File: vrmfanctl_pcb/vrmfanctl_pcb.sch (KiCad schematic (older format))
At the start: 6 parts, among them J1 SATA Power Male, J2 Conn_02x03_Odd_Even, J3 Pin socket L-shape, J4 Pin socket L-shape, U1 ATtiny85-20PU

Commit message: change temperature measurement method. remove configuration interface. use printf instead of put*.
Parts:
- removed J2: Conn_02x03_Odd_Even, symbol Connector_Generic:Conn_02x03_Odd_Even
- added C2: 470p, Capacitor_THT:C_Disc_D3.0mm_W1.6mm_P2.50mm, symbol Device:C_Small
- added Q1, Q2, Q3: 2SC1740, Package_TO_SOT_THT:TO-92_Inline_Wide, symbol Device:Q_NPN_ECB
- added R1: 56k, Resistor_THT:R_Axial_DIN0204_L3.6mm_D1.6mm_P5.08mm_Horizontal, symbol Device:R
- added R2, R3: 390k, Resistor_THT:R_Axial_DIN0204_L3.6mm_D1.6mm_P5.08mm_Horizontal, symbol Device:R
- added R4: 20k, Resistor_THT:R_Axial_DIN0204_L3.6mm_D1.6mm_P5.08mm_Horizontal, symbol Device:R
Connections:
- net labels added: BDPWR10, BDPWR200, D-
- net labels removed: FG, RX
- wire segments 47 -> 78
- no-connect marks 10 -> 11
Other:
- note added: "1x/about 20.1x"
- moved on the sheet: J3, J4

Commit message: swap BDPWR10 and TX. Add UART pin header
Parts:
- added J2: Pin header L-shape, Connector_PinHeader_2.54mm:PinHeader_1x02_P2.54mm_Horizontal, symbol Connector:Conn_01x02_Male
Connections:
- net TX is gone; now on net BDPWR10: U1.1 (~RESET~/PB5)
- net BDPWR10: no longer U1.5 (AREF/PB0)
- net GND: now also J2.2 (Pin_2)
- new net TX_RX: J2.1 (Pin_1), U1.5 (AREF/PB0)
- no-connect marks 11 -> 10
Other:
- note removed: "1x/about 20.1x"
- moved on the sheet: J4
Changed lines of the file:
@@
 EESchema Schematic File Version 4
 LIBS:vrmfanctl_pcb-cache
-EELAYER 30 0
+EELAYER 26 0
 EELAYER END
 $Descr A4 11693 8268
@@
 	1    0    0    -1
 $EndComp
-Text Notes 6100 1100 0    50   ~ 0
+Text Notes 7300 700  0    50   ~ 0
 PWM(BLUE)
-Text Notes 6100 1200 0    50   ~ 0
+Text Notes 7300 800  0    50   ~ 0
 FOO(YELLOW)
-Text Notes 6100 1300 0    50   ~ 0
+Text Notes 7300 900  0    50   ~ 0
 V-(BLACK)
-Text Notes 6100 1400 0    50   ~ 0
+Text Notes 7300 1000 0    50   ~ 0
 V+(RED)
-Text Notes 6100 1000 0    50   ~ 0
+Text Notes 7300 600  0    50   ~ 0
 To Fan (KDB0305HA3-CD7)
 Wire Wire Line
-	5700 1250 5850 1250
-Wire Wire Line
-	5700 1250 5700 1300
+	6900 850  7050 850
+Wire Wire Line
+	6900 850  6900 900
 Wire Wire Line
 	4500 1350 4500 1500
 Wire Wire Line
-	5800 1350 5850 1350
+	7000 950  7050 950
 Text Notes 1100 2050 0    50   ~ 0
 5V±5%
@@
 $EndComp
 Wire Wire Line
-	5800 1350 5800 1500
+	7000 950  7000 1100
 Wire Wire Line
 	3800 1250 3800 1350
@@
 L power:GND #PWR07
 U 1 1 5D5E75C4
-P 5700 1300
-F 0 "#PWR07" H 5700 1050 50  0001 C CNN
-F 1 "GND" H 5705 1127 50  0000 C CNN
-F 2 "" H 5700 1300 50  0001 C CNN
-F 3 "" H 5700 1300 50  0001 C CNN
-	1    5700 1300
+P 6900 900
+F 0 "#PWR07" H 6900 650 50  0001 C CNN
+F 1 "GND" H 6905 727 50  0000 C CNN
+F 2 "" H 6900 900 50  0001 C CNN
+F 3 "" H 6900 900 50  0001 C CNN
+	1    6900 900
 	1    0    0    -1
 $EndComp
@@
 L power:VCC #PWR08
 U 1 1 5D5EAA48
-P 5800 1500
-F 0 "#PWR08" H 5800 1350 50  0001 C CNN
-F 1 "VCC" H 5818 1673 50  0000 C CNN
-F 2 "" H 5800 1500 50  0001 C CNN
-F 3 "" H 5800 1500 50  0001 C CNN
-	1    5800 1500
+P 7000 1100
+F 0 "#PWR08" H 7000 950 50  0001 C CNN
+F 1 "VCC" H 7018 1273 50  0000 C CNN
+F 2 "" H 7000 1100 50  0001 C CNN
+F 3 "" H 7000 1100 50  0001 C CNN
+	1    7000 1100
 	-1   0    0    1
 $EndComp
@@
 L Connector:Conn_01x04_Female J4
 U 1 1 5D5F6860
-P 6050 1150
-F 0 "J4" H 6100 800 50  0000 L CNN
-F 1 "Pin socket L-shape" H 6100 700 50  0000 L CNN
-F 2 "Connector_PinSocket_2.54mm:PinSocket_1x04_P2.54mm_Horizontal" H 6050 1150 50  0001 C CNN
-F 3 "~" H 6050 1150 50  0001 C CNN
-	1    6050 1150
-	1    0    0    -1
-$EndComp
-NoConn ~ 5100 2300
+P 7250 750
+F 0 "J4" H 7300 400 50  0000 L CNN
+F 1 "Pin socket L-shape" H 7300 300 50  0000 L CNN
+F 2 "Connector_PinSocket_2.54mm:PinSocket_1x04_P2.54mm_Horizontal" H 7250 750 50  0001 C CNN
+F 3 "~" H 7250 750 50  0001 C CNN
+	1    7250 750
+	1    0    0    -1
+$EndComp
 Text Label 5100 1900 0    50   ~ 0
 PWM
@@
 	1    0    0    -1
 $EndComp
-NoConn ~ 5850 1150
-Wire Wire Line
-	5850 1050 5600 1050
+NoConn ~ 7050 750
 Wire Wire Line
 	5600 1900 5100 1900
@@
 Wire Wire Line
 	6200 4050 6550 4050
-Text Label 5100 1800 0    50   ~ 0
+Text Label 5100 2300 0    50   ~ 0
 BDPWR10
 Wire Wire Line
@@
 	5400 2000 5400 4250
 Wire Wire Line
-	5600 1050 5600 1900
-Wire Wire Line
-	5100 1800 5500 1800
-Wire Wire Line
-	5500 1800 5500 4150
-Wire Wire Line
 	6550 3450 6550 3600
 $Comp
@@
 Wire Wire Line
 	5850 3000 5850 3050
-Text Notes 7400 3300 0    50   ~ 0
-1x/about 20.1x
-Text Label 5100 2300 0    50   ~ 0
-TX
+Text Label 5100 1800 0    50   ~ 0
+TX_RX
+$Comp
+L Connector:Conn_01x02_Male J2
+U 1 1 5D999CB1
+P 7250 1600
+F 0 "J2" H 7222 1480 50  0000 R CNN
+F 1 "Pin header L-shape" H 7222 1571 50  0000 R CNN
+F 2 "Connector_PinHeader_2.54mm:PinHeader_1x02_P2.54mm_Horizontal" H 7250 1600 50  0001 C CNN
+F 3 "~" H 7250 1600 50  0001 C CNN
+	1    7250 1600
+	-1   0    0    -1
+$EndComp
+Wire Wire Line
+	5600 650  5600 1900
+Wire Wire Line
+	5600 650  7050 650
+Wire Wire Line
+	5100 2300 5500 2300
+Wire Wire Line
+	5500 2300 5500 4150
+Wire Wire Line
+	5100 1800 5700 1800
+Wire Wire Line
+	5700 1800 5700 1600
+Wire Wire Line
+	5700 1600 7050 1600
+$Comp
+L power:GND #PWR0104
+U 1 1 5D9A1D78
+P 6950 1800
+F 0 "#PWR0104" H 6950 1550 50  0001 C CNN
+F 1 "GND" H 6955 1627 50  0000 C CNN
+F 2 "" H 6950 1800 50  0001 C CNN
+F 3 "" H 6950 1800 50  0001 C CNN
+	1    6950 1800
+	1    0    0    -1
+$EndComp
+Wire Wire Line
+	7050 1700 6950 1700
+Wire Wire Line
+	6950 1700 6950 1800
 $EndSCHEMATC

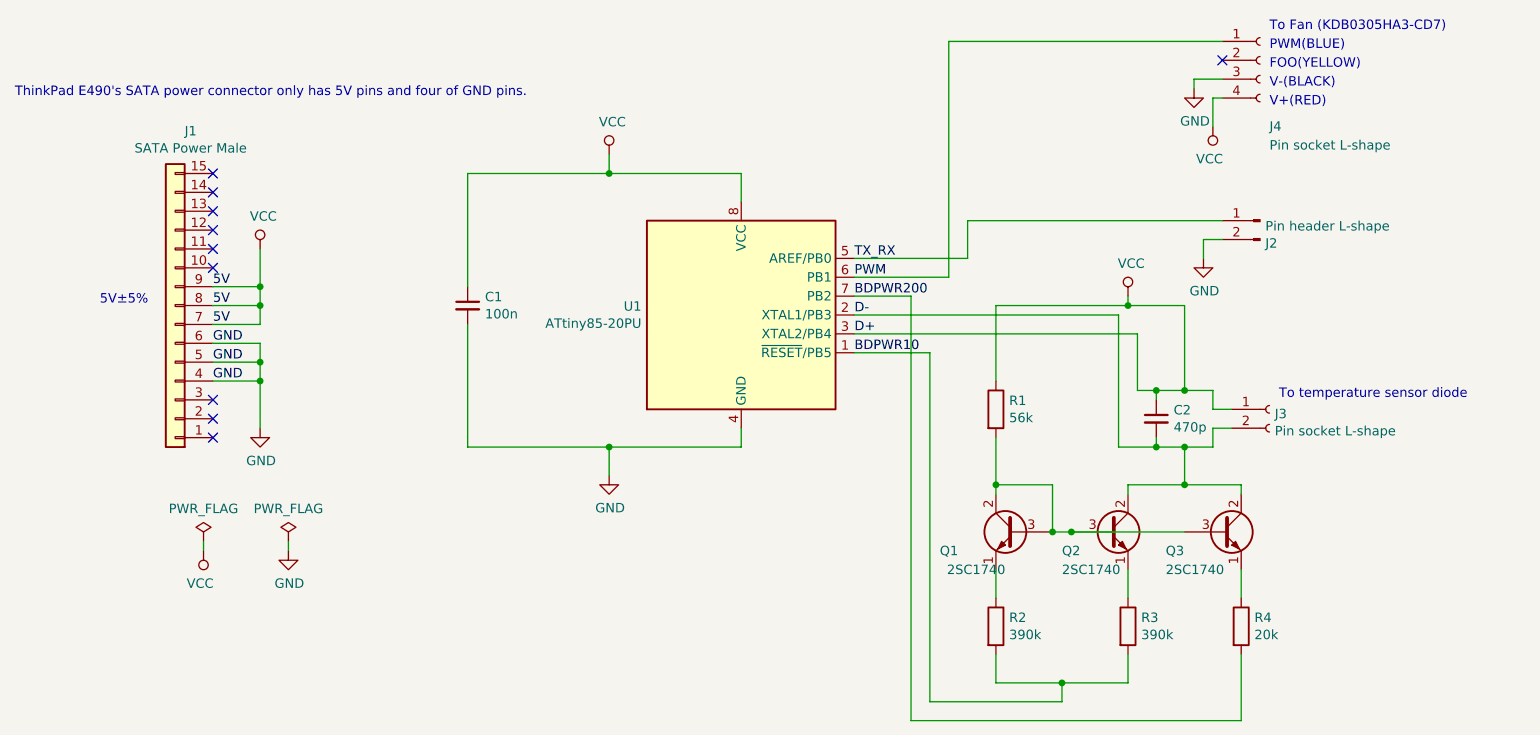
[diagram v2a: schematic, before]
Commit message: keep analog signals from digital signals
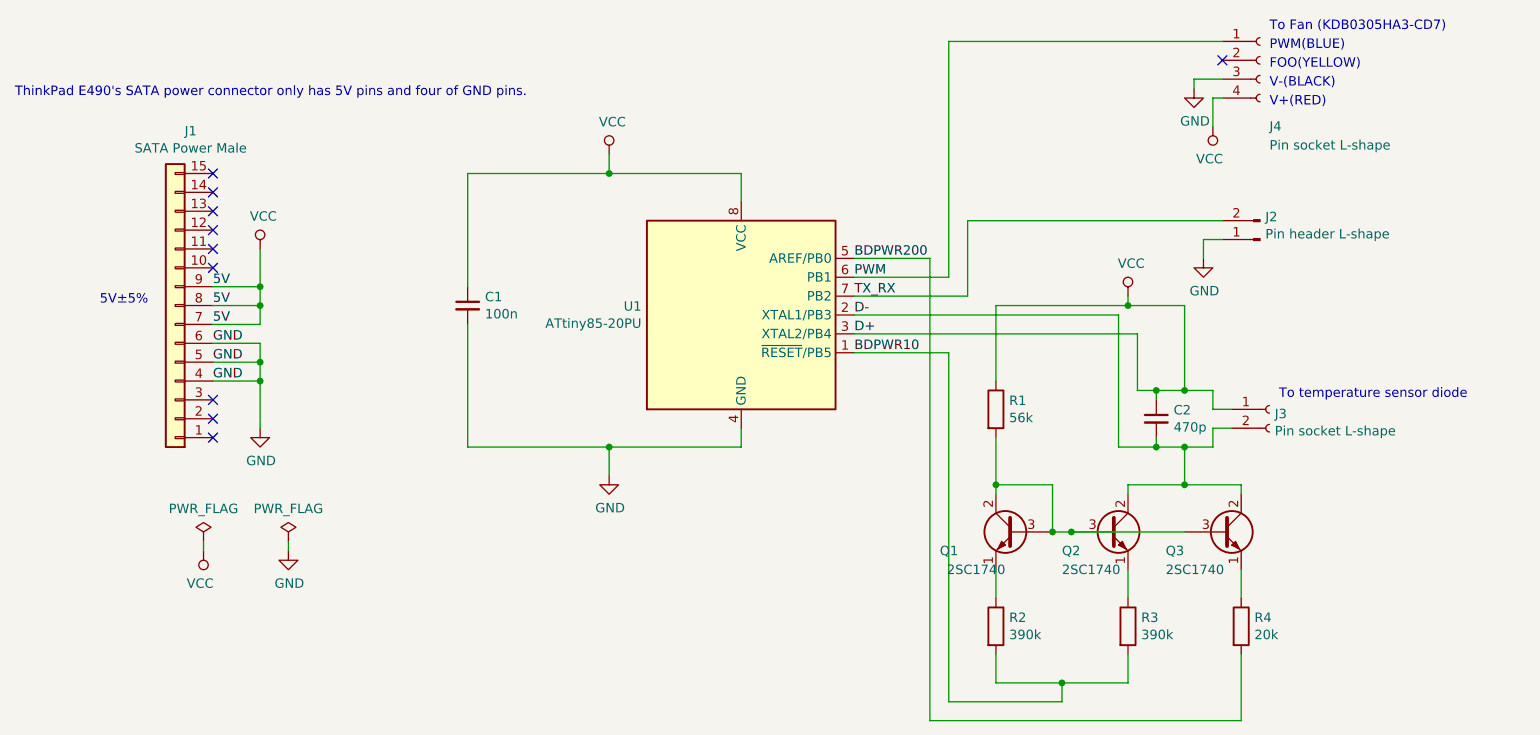
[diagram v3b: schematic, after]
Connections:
- net BDPWR200: now also U1.5 (AREF/PB0); no longer U1.7 (PB2)
- net GND: now also J2.1 (Pin_1); no longer J2.2 (Pin_2)
- net TX_RX: now also J2.2 (Pin_2), U1.7 (PB2); no longer J2.1 (Pin_1), U1.5 (AREF/PB0)
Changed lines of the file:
@@
 EESchema Schematic File Version 4
 LIBS:vrmfanctl_pcb-cache
-EELAYER 26 0
+EELAYER 30 0
 EELAYER END
 $Descr A4 11693 8268
@@
 Wire Wire Line
 	7150 3900 7150 4250
-Text Label 5100 2000 0    50   ~ 0
+Text Label 5100 1800 0    50   ~ 0
 BDPWR200
 Wire Wire Line
@@
 	6850 2500 7000 2500
 Wire Wire Line
-	5100 2000 5400 2000
-Wire Wire Line
-	5400 2000 5400 4250
-Wire Wire Line
 	6550 3450 6550 3600
 $Comp
@@
 	5850 3900 5850 4050
 Wire Wire Line
-	5500 4150 6200 4150
-Wire Wire Line
-	5400 4250 7150 4250
+	5600 4150 6200 4150
+Wire Wire Line
+	5500 4250 7150 4250
 Wire Wire Line
 	5100 2100 6500 2100
@@
 Wire Wire Line
 	5850 3000 5850 3050
-Text Label 5100 1800 0    50   ~ 0
+Text Label 5100 2000 0    50   ~ 0
 TX_RX
 $Comp
 L Connector:Conn_01x02_Male J2
 U 1 1 5D999CB1
-P 7250 1600
-F 0 "J2" H 7222 1480 50  0000 R CNN
-F 1 "Pin header L-shape" H 7222 1571 50  0000 R CNN
-F 2 "Connector_PinHeader_2.54mm:PinHeader_1x02_P2.54mm_Horizontal" H 7250 1600 50  0001 C CNN
-F 3 "~" H 7250 1600 50  0001 C CNN
-	1    7250 1600
-	-1   0    0    -1
+P 7250 1700
+F 0 "J2" H 7222 1580 50  0000 R CNN
+F 1 "Pin header L-shape" H 7222 1671 50  0000 R CNN
+F 2 "Connector_PinHeader_2.54mm:PinHeader_1x02_P2.54mm_Horizontal" H 7250 1700 50  0001 C CNN
+F 3 "~" H 7250 1700 50  0001 C CNN
+	1    7250 1700
+	-1   0    0    1
 $EndComp
 Wire Wire Line
@@
 	5600 650  7050 650
 Wire Wire Line
-	5100 2300 5500 2300
-Wire Wire Line
-	5500 2300 5500 4150
-Wire Wire Line
-	5100 1800 5700 1800
-Wire Wire Line
-	5700 1800 5700 1600
+	5100 2300 5600 2300
+Wire Wire Line
+	5600 2300 5600 4150
 Wire Wire Line
 	5700 1600 7050 1600
@@
 Wire Wire Line
 	6950 1700 6950 1800
+Wire Wire Line
+	5100 1800 5500 1800
+Wire Wire Line
+	5500 1800 5500 4250
+Wire Wire Line
+	5100 2000 5700 2000
+Wire Wire Line
+	5700 1600 5700 2000
 $EndSCHEMATC

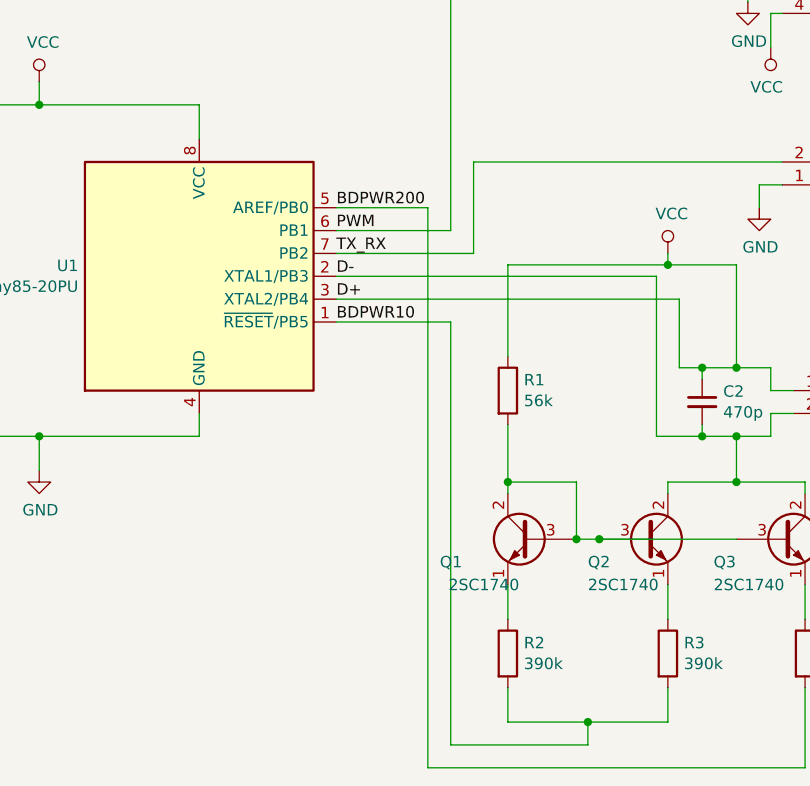
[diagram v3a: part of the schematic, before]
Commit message: swap PB2 and PB0
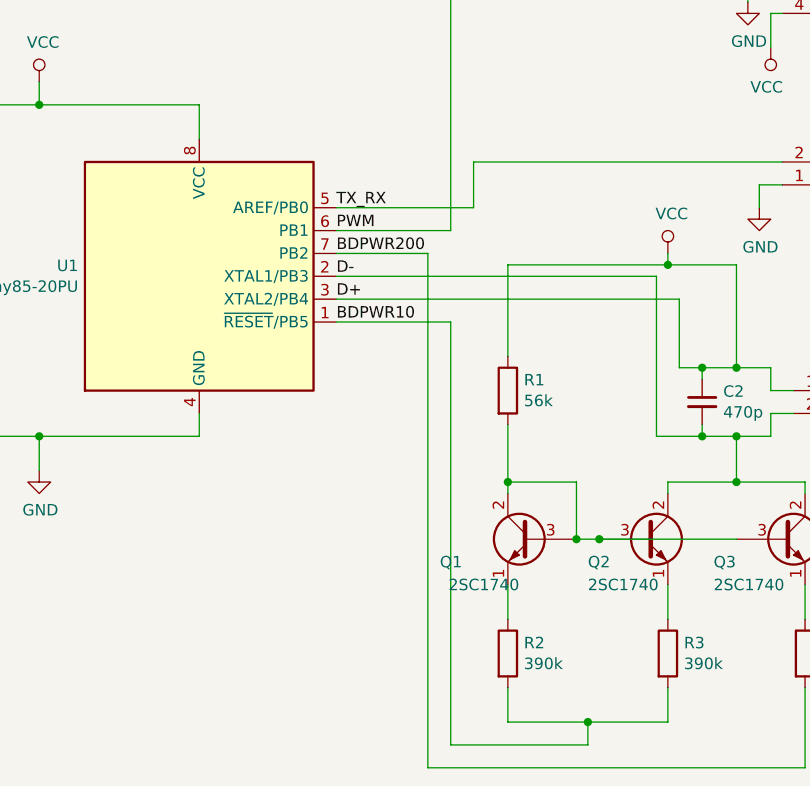
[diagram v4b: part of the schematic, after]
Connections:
- net BDPWR200: now also U1.7 (PB2); no longer U1.5 (AREF/PB0)
- net TX_RX: now also U1.5 (AREF/PB0); no longer U1.7 (PB2)
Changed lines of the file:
@@
 EESchema Schematic File Version 4
 LIBS:vrmfanctl_pcb-cache
-EELAYER 30 0
+EELAYER 26 0
 EELAYER END
 $Descr A4 11693 8268
@@
 Wire Wire Line
 	7150 3900 7150 4250
-Text Label 5100 1800 0    50   ~ 0
+Text Label 5100 2000 0    50   ~ 0
 BDPWR200
 Wire Wire Line
@@
 Wire Wire Line
 	5850 3000 5850 3050
-Text Label 5100 2000 0    50   ~ 0
+Text Label 5100 1800 0    50   ~ 0
 TX_RX
 $Comp
@@
 	6950 1700 6950 1800
 Wire Wire Line
-	5100 1800 5500 1800
-Wire Wire Line
-	5500 1800 5500 4250
-Wire Wire Line
-	5100 2000 5700 2000
-Wire Wire Line
-	5700 1600 5700 2000
+	5700 1600 5700 1800
+Wire Wire Line
+	5100 2000 5500 2000
+Wire Wire Line
+	5500 2000 5500 4250
+Wire Wire Line
+	5100 1800 5700 1800
 $EndSCHEMATC

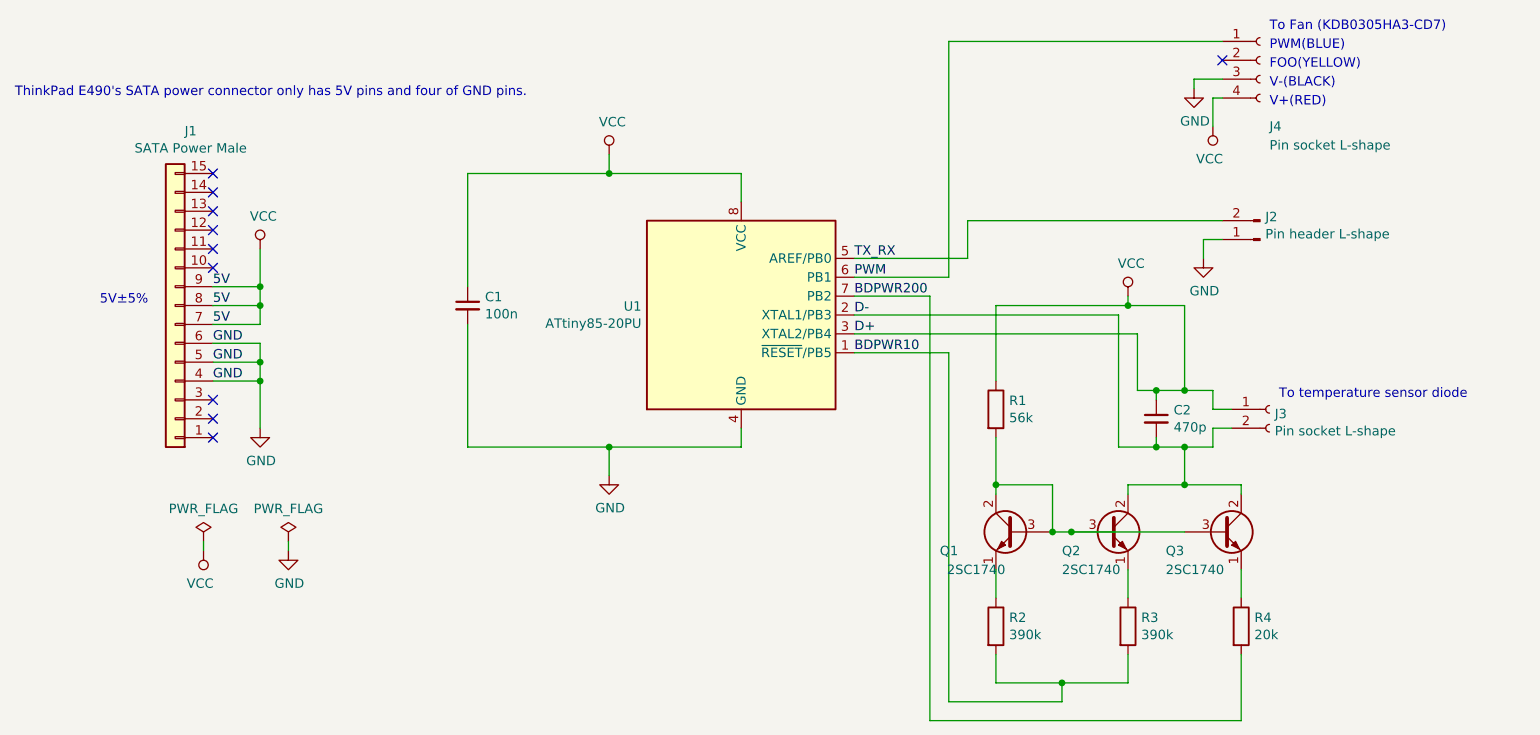
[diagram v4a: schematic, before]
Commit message: use thermistor instead of thermal diode
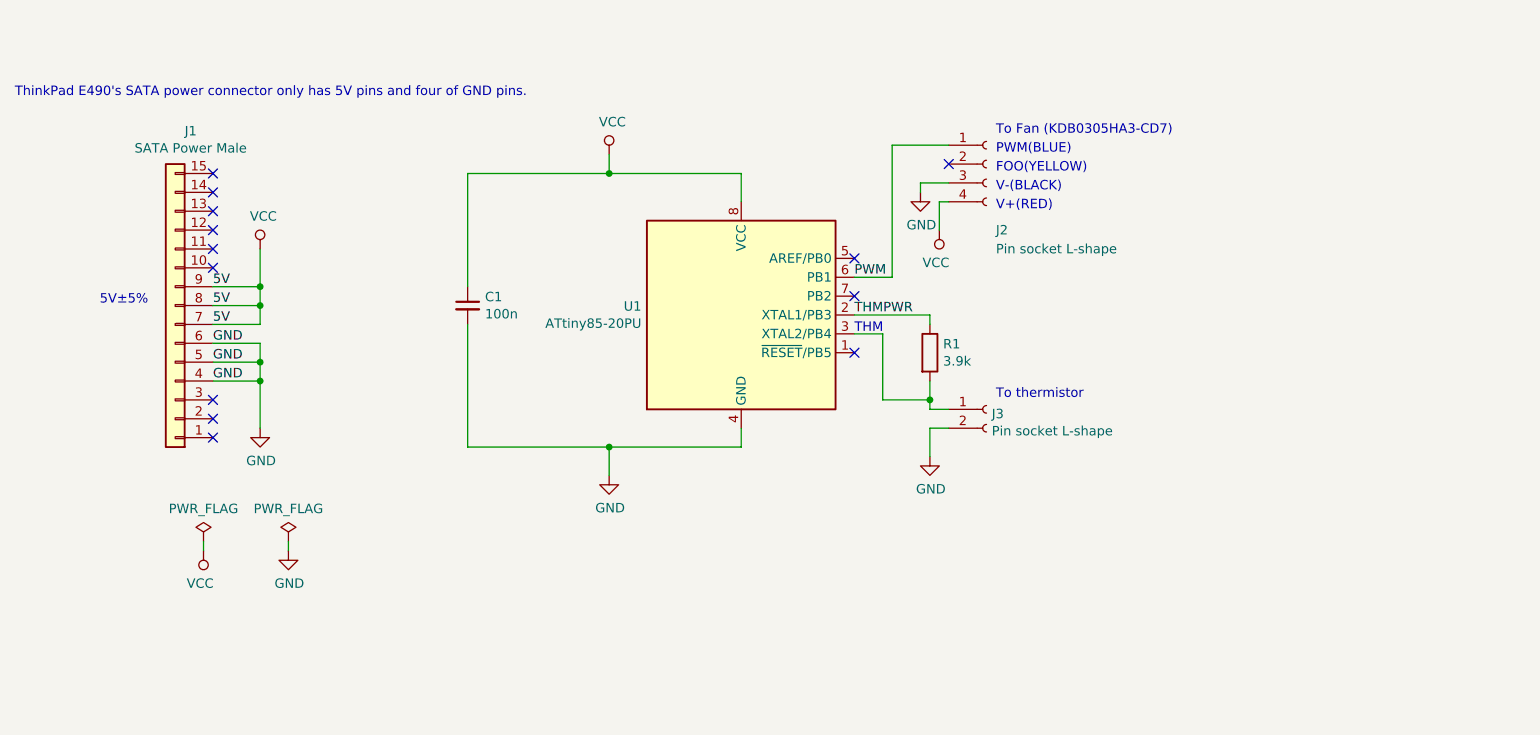
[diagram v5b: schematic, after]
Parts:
- removed C2: 470p, Capacitor_THT:C_Disc_D3.0mm_W1.6mm_P2.50mm, symbol Device:C_Small
- removed J2: Pin header L-shape, Connector_PinHeader_2.54mm:PinHeader_1x02_P2.54mm_Horizontal, symbol Connector:Conn_01x02_Male
- removed Q1, Q2, Q3: 2SC1740, Package_TO_SOT_THT:TO-92_Inline_Wide, symbol Device:Q_NPN_ECB
- removed R2, R3: 390k, Resistor_THT:R_Axial_DIN0204_L3.6mm_D1.6mm_P5.08mm_Horizontal, symbol Device:R
- removed R4: 20k, Resistor_THT:R_Axial_DIN0204_L3.6mm_D1.6mm_P5.08mm_Horizontal, symbol Device:R
- R1: value 56k -> 3.9k
- renumbered J4 to J2
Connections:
- net GND: now also J3.2 (Pin_2)
- net VCC: no longer J3.1 (Pin_1), R1.1, U1.3 (XTAL2/PB4)
- net at R1.2: now also J3.1 (Pin_1), U1.3 (XTAL2/PB4)
- net BDPWR10: no longer names the net of U1.1 (~RESET~/PB5)
- net BDPWR200: no longer names the net of U1.7 (PB2)
- net D- renamed THMPWR
- net THMPWR: now also R1.1; no longer J3.2 (Pin_2)
- net TX_RX: no longer names the net of U1.5 (AREF/PB0)
- no-connect marks 10 -> 13
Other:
- note added: "THM"
- note added: "To thermistor"
- note removed: "To temperature sensor diode"
- moved on the sheet: J2, J3

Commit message: update pcb layout
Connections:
- net TX_RX: now reaches U1.5 (AREF/PB0)
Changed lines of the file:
@@
 	5250 2200 5100 2200
 Wire Wire Line
-	5600 1200 5300 1200
+	5600 1200 5350 1200
 Wire Wire Line
-	5300 1200 5300 1900
+	5350 1200 5350 1900
 Wire Wire Line
-	5300 1900 5100 1900
+	5350 1900 5100 1900
 Wire Wire Line
 	5500 2550 5500 2600
@@
 Text Notes 5100 2200 0    50   ~ 0
 THM
+Text Label 5100 1800 0    50   ~ 0
+TX_RX
 $EndSCHEMATC
